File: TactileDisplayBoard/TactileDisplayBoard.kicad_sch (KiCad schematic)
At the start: 12 parts, among them J1 Conn_01x02, J2 Conn_01x02, J3 Microstep_Jumper, J4 Conn_Motor, J5 Microstep_Jumper, J6 Conn_Motor, J7 PowerSwitch, U1 A4988, U2 ESP32-DEVKITC, U3 A4988

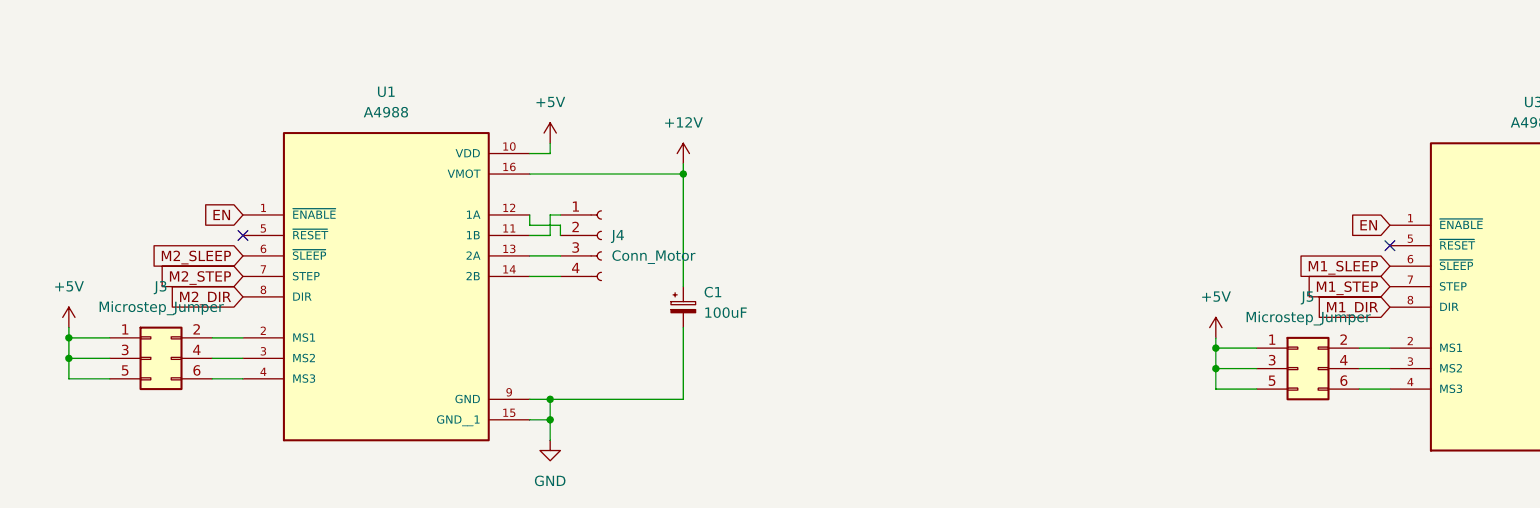
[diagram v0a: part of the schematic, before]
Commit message: Added BLE, and wrote firmware for ESP32 in Display Driver
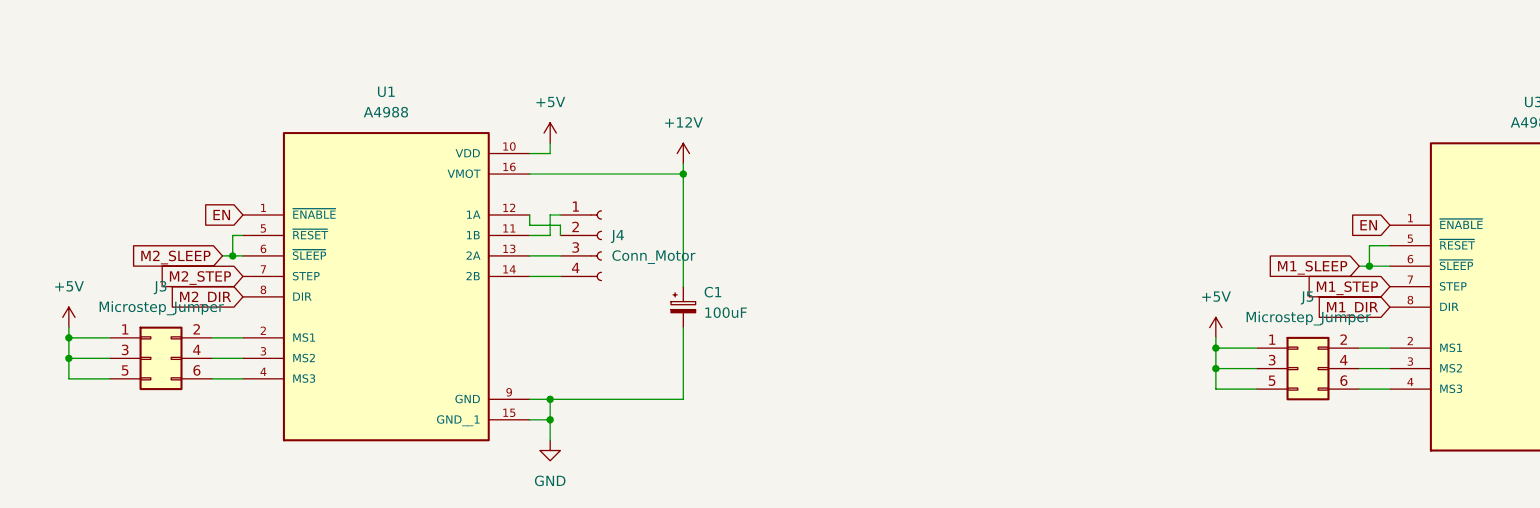
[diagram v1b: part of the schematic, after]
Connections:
- net M1_SLEEP: now also U3.5 (~{RESET})
- net M2_SLEEP: now also U1.5 (~{RESET})
- no-connect marks 28 -> 26
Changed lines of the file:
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@@
   (junction (at 105.41 99.06) (diameter 0) (color 0 0 0 0)
   )
+  (junction (at 190.5 110.49) (diameter 0) (color 0 0 0 0)
+  )
   (junction (at 29.21 119.38) (diameter 0) (color 0 0 0 0)
   )
+  (junction (at 49.53 109.22) (diameter 0) (color 0 0 0 0)
+  )
   (junction (at 88.9 129.54) (diameter 0) (color 0 0 0 0)
   )
-  (no_connect (at 50.8 106.68))
-  (no_connect (at 193.04 107.95))
   (no_connect (at 107.95 38.1))
   (no_connect (at 107.95 40.64))
@@
     (stroke (width 0) (type default) (color 0 0 0 0))
   )
+  (wire (pts (xy 189.23 110.49) (xy 190.5 110.49))
+    (stroke (width 0) (type default) (color 0 0 0 0))
+  )
   (wire (pts (xy 105.41 113.03) (xy 105.41 99.06))
     (stroke (width 0) (type default) (color 0 0 0 0))
@@
     (stroke (width 0) (type default) (color 0 0 0 0))
   )
+  (wire (pts (xy 48.26 109.22) (xy 49.53 109.22))
+    (stroke (width 0) (type default) (color 0 0 0 0))
+  )
   (wire (pts (xy 34.29 39.37) (xy 38.1 39.37))
     (stroke (width 0) (type default) (color 0 0 0 0))
@@
     (stroke (width 0) (type default) (color 0 0 0 0))
   )
+  (wire (pts (xy 190.5 110.49) (xy 193.04 110.49))
+    (stroke (width 0) (type default) (color 0 0 0 0))
+  )
+  (wire (pts (xy 193.04 107.95) (xy 190.5 107.95))
+    (stroke (width 0) (type default) (color 0 0 0 0))
+  )
   (wire (pts (xy 46.99 124.46) (xy 50.8 124.46))
     (stroke (width 0) (type default) (color 0 0 0 0))
@@
     (stroke (width 0) (type default) (color 0 0 0 0))
   )
+  (wire (pts (xy 49.53 109.22) (xy 50.8 109.22))
+    (stroke (width 0) (type default) (color 0 0 0 0))
+  )
+  (wire (pts (xy 49.53 106.68) (xy 49.53 109.22))
+    (stroke (width 0) (type default) (color 0 0 0 0))
+  )
   (wire (pts (xy 247.65 128.27) (xy 231.14 128.27))
     (stroke (width 0) (type default) (color 0 0 0 0))
@@
     (stroke (width 0) (type default) (color 0 0 0 0))
   )
+  (wire (pts (xy 190.5 107.95) (xy 190.5 110.49))
+    (stroke (width 0) (type default) (color 0 0 0 0))
+  )
   (wire (pts (xy 232.41 107.95) (xy 231.14 107.95))
     (stroke (width 0) (type default) (color 0 0 0 0))
@@
   )
   (wire (pts (xy 105.41 97.79) (xy 105.41 99.06))
+    (stroke (width 0) (type default) (color 0 0 0 0))
+  )
+  (wire (pts (xy 50.8 106.68) (xy 49.53 106.68))
     (stroke (width 0) (type default) (color 0 0 0 0))
   )
@@
     )
   )
-  (global_label "M2_SLEEP" (shape input) (at 50.8 109.22 180) (fields_autoplaced)
+  (global_label "M2_SLEEP" (shape input) (at 48.26 109.22 180) (fields_autoplaced)
     (effects (font (size 1.27 1.27)) (justify right))
-    (property "Intersheet References" "${INTERSHEET_REFS}" (id 0) (at 38.9526 109.1406 0)
+    (property "Intersheet References" "${INTERSHEET_REFS}" (id 0) (at 36.4126 109.1406 0)
       (effects (font (size 1.27 1.27)) (justify right) hide)
     )
@@
     )
   )
-  (global_label "M1_SLEEP" (shape input) (at 193.04 110.49 180) (fields_autoplaced)
+  (global_label "M1_SLEEP" (shape input) (at 189.23 110.49 180) (fields_autoplaced)
     (effects (font (size 1.27 1.27)) (justify right))
-    (property "Intersheet References" "${INTERSHEET_REFS}" (id 0) (at 181.1926 110.4106 0)
+    (property "Intersheet References" "${INTERSHEET_REFS}" (id 0) (at 177.3826 110.4106 0)
       (effects (font (size 1.27 1.27)) (justify right) hide)
     )

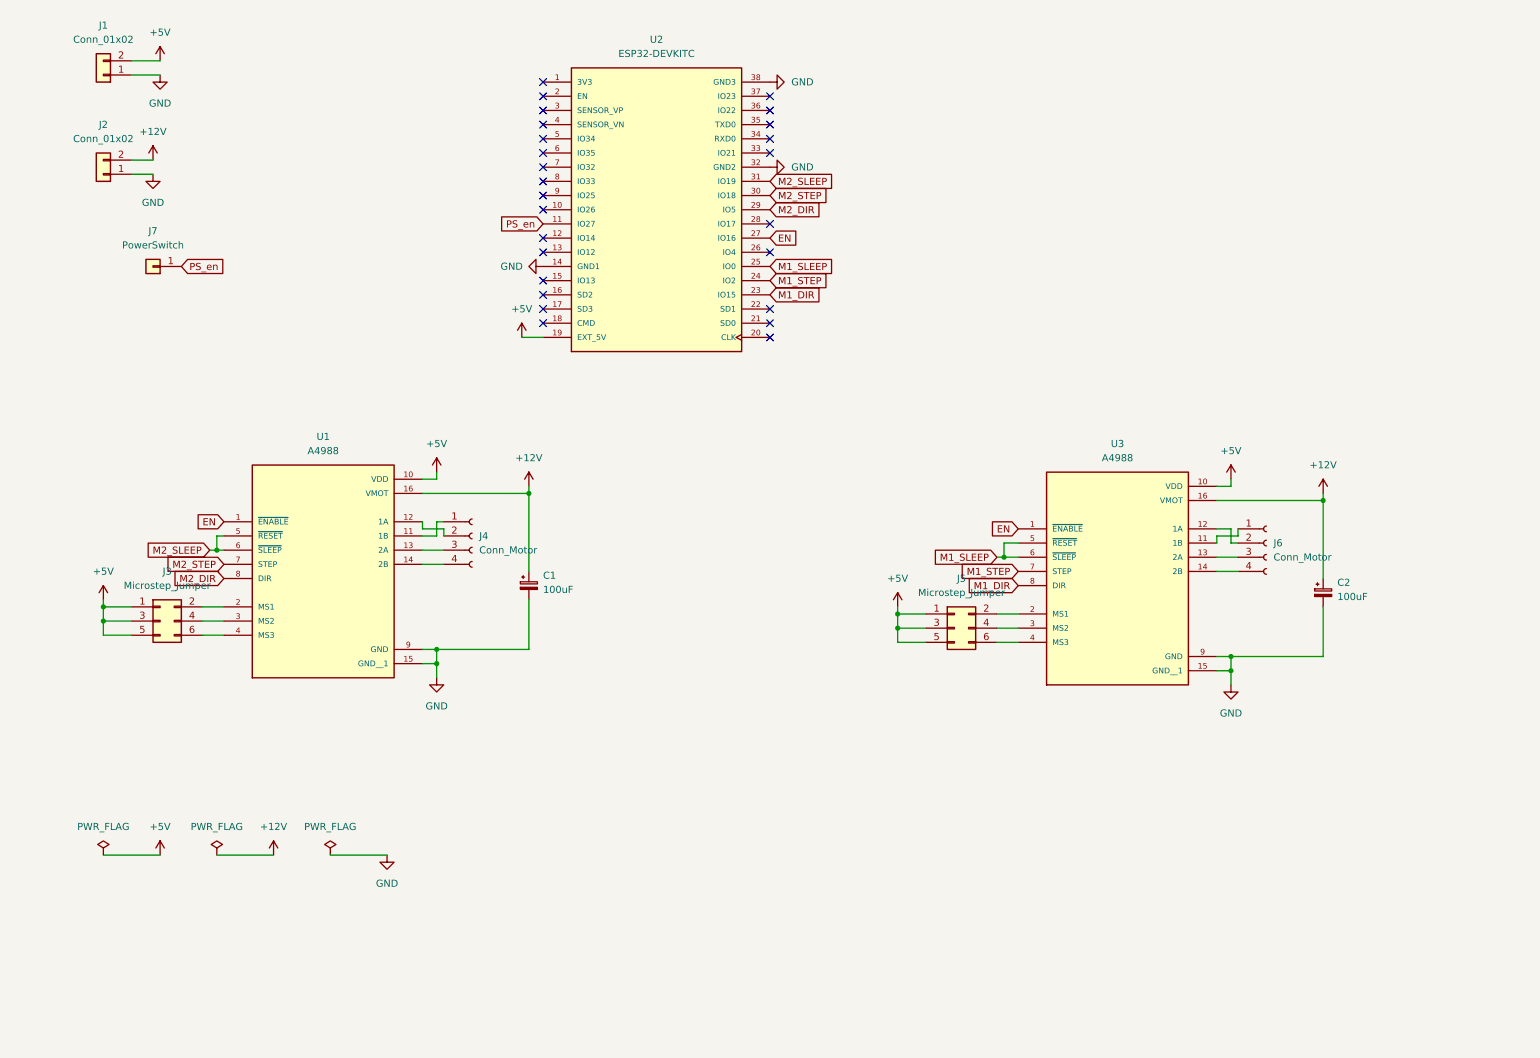
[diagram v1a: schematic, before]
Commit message: Adjusted wheel number and added shutoff system.
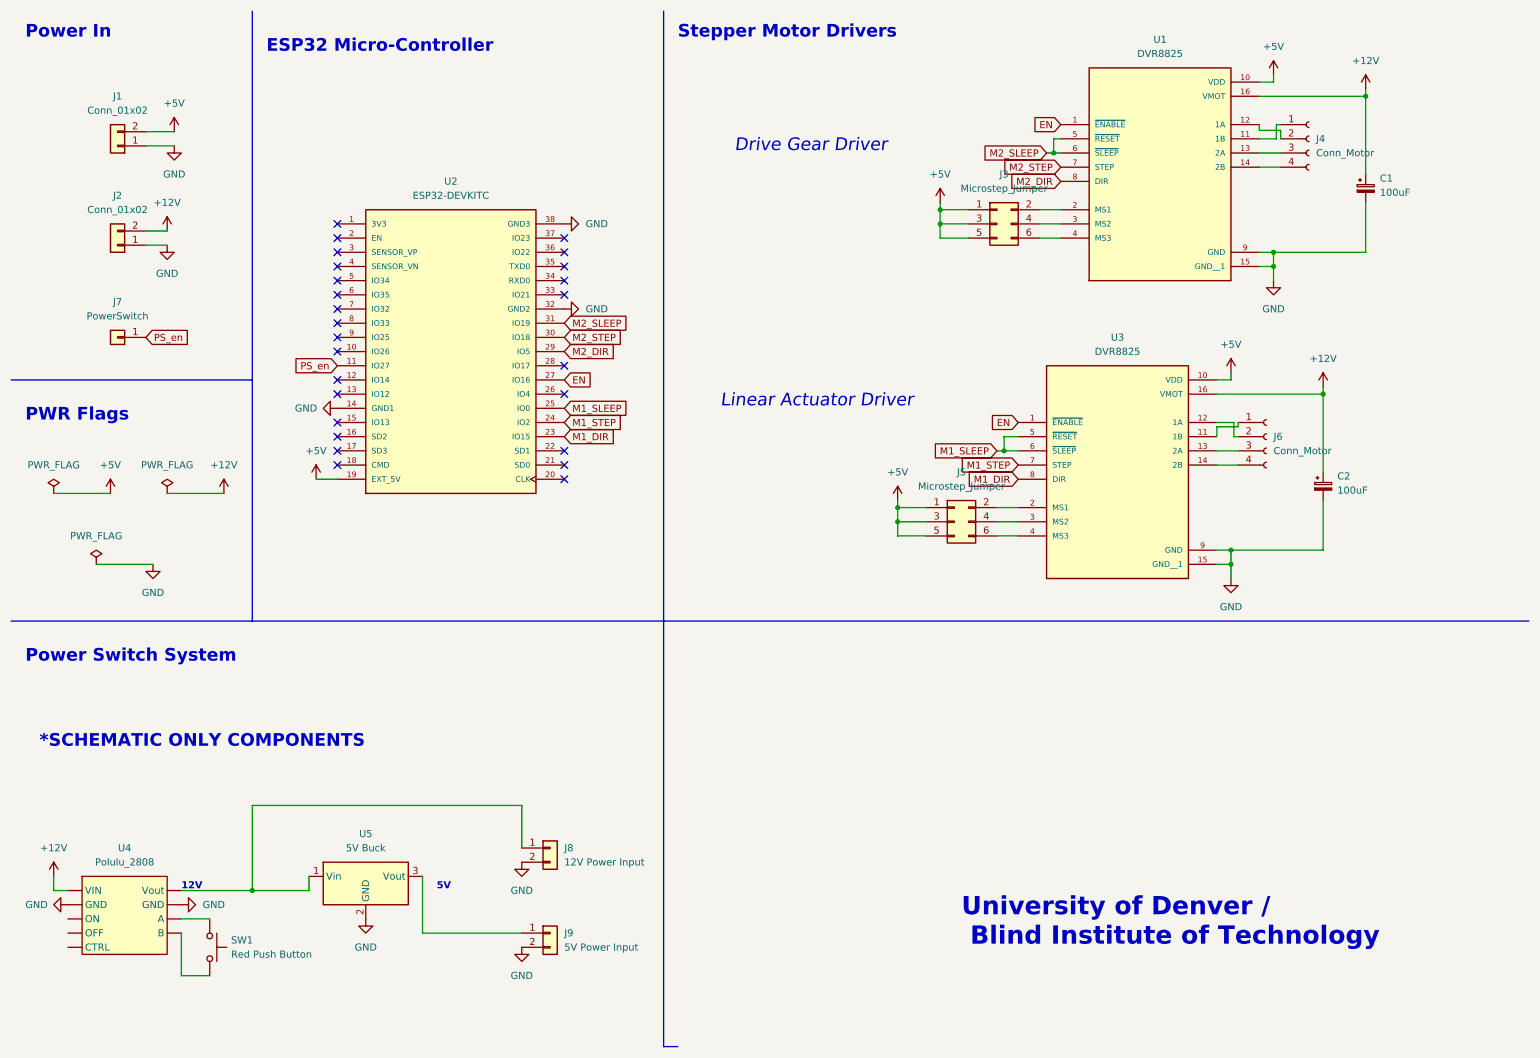
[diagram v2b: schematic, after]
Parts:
- added J8: 12V Power Input, Connector_BarrelJack:BarrelJack_CUI_PJ-102AH_Horizontal, symbol Connector_Generic:Conn_01x02
- added J9: 5V Power Input, Connector_BarrelJack:BarrelJack_CUI_PJ-102AH_Horizontal, symbol Connector_Generic:Conn_01x02
- added SW1: Red Push Button, symbol Switch:SW_Push
- added U4: Polulu_2808, symbol A4988_STEPPER_MOTOR_DRIVER_CARRIER:Polulu_2808
- added U5: 5V Buck, Converter_DCDC:Converter_DCDC_TRACO_TSR-1_THT, symbol Regulator_Switching:TSR_1-24150
- U1, U3: value A4988 -> DVR8825
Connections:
- net +12V: now also U4. (Vout)
- net GND: now also J8.2 (Pin_2), J9.2 (Pin_2), U4. (Vout), U5.2 (GND)
- new net: J8.1 (Pin_1), U4. (Vout), U5.1 (Vin)
- new net: J9.1 (Pin_1), U5.3 (Vout)
- new net: SW1.1, U4. (Vout)
- new net: SW1.2, U4. (Vout)
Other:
- note added: "*SCHEMATIC ONLY COMPONENTS"
- note added: "12V"
- note added: "5V"
- note added: "Drive Gear Driver"
- note added: "ESP32 Micro-Controller"
- note added: "Linear Actuator Driver"
- note added: "PWR Flags"
- note added: "Power In"
- note added: "Power Switch System"
- note added: "Stepper Motor Drivers"
- note added: "University of Denver / Blind Institute of Technology"
- title: (none) -> Tactile Display Board
- moved on the sheet: C1, C2, J1, J2, J3, J4, J5, J6, J7, U1, U2, U3
